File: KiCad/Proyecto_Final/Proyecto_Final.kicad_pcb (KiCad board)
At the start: 4 copper layers, 102 x 102 mm, 231 parts, among them J1 RF_IN, J10 PB, J11 PE, J12 PA, J13 PD, J14 SPI4, J15 OutEn, J16 CFG_SEL, J17 CTRL_MODE, J2 5v, J3 I2C1, J4 ARM SWD, J5 USB_B_Micro, J6 Boot_Select, J7 PG, J8 PC, J9 PF, Q1 Si2301CDS, SW1 Reset, T1 B0310J50100AHF, T2 B0310J50100AHF, T3 2450BL05A0100, U1 SKY13351, U10 MAX2837, U11 TLV1117-33, U12 USBLC6-2SC6, U13 STM32F723ZCTx, U14 5P49V5929, U2 RFFC5072, U3 SKY13351, U4 SKY13351, U5 SKY13351, U6 SKY13351, U7 SKY13351, U8 MAAL-010200, U9 MAX1193ETI+, Y1 25MHz

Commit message: Avances PCB.
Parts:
- removed J17: CTRL_MODE, Connector_PinHeader_2.54mm:PinHeader_2x01_P2.54mm_Vertical_SMD
- removed the R26 at (87.0, 53.6)
- removed R27, R28: 10k, Resistor_SMD:R_0402_1005Metric
- added H1: MountingHole, MountingHole:MountingHole_3.2mm_M3_Pad_Via, F.Cu at (53.6, 90.7)
- added H2: MountingHole, MountingHole:MountingHole_3.2mm_M3_Pad_Via, F.Cu at (80.0, 145.2)
- added H3: MountingHole, MountingHole:MountingHole_3.2mm_M3_Pad_Via, F.Cu at (61.5, 90.7)
- added H4: MountingHole, MountingHole:MountingHole_3.2mm_M3_Pad_Via, F.Cu at (171.3, 145.2)
- added JP1: SolderJumper, Jumper:SolderJumper-2_P1.3mm_Open_RoundedPad1.0x1.5mm, F.Cu at (127.1, 104.3)
- J16: value CFG_SEL -> CLK_OUT0; footprint Connector_PinHeader_2.54mm:PinHeader_2x04_P2.54mm_Vertical_SMD -> Tesis2020-21:RFSOLUTIONS_CON-SMA-EDGE-S
- R17, R18: value 10k -> 4.7k
- moved U11 98.2 mm to (96.4, 104.0)
- moved J3 76.3 mm to (154.0, 88.6), turned to 180 degrees
- moved J6 72.5 mm to (142.7, 78.9)
- moved R17 57.9 mm to (154.2, 91.2)
- moved R18 56.9 mm to (153.5, 92.3)
- moved J4 56.6 mm to (114.6, 79.0)
- moved J14 49.3 mm to (137.9, 67.0)
- moved J16 33.5 mm to (125.4, 78.4), turned to 270 degrees
- moved J15 19.7 mm to (114.2, 112.2), turned to 180 degrees
- moved U12 9.70 mm to (161.0, 139.1), turned to 90 degrees
- moved J5 8.95 mm to (160.2, 146.5)
- moved C109 6.35 mm to (119.8, 102.5), turned to 225 degrees
- moved R26 4.83 mm to (127.1, 100.9), turned to 90 degrees
- moved C110 4.81 mm to (119.3, 106.5), turned to 135 degrees
- moved R24 0.39 mm to (121.2, 111.8), turned to 45 degrees
- renumbered R29 to R26
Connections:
- J16 pad 2: Net-(J16-Pad1) -> GND
- R26 pad 1: Net-(R29-Pad1) -> Net-(JP1-Pad2)
- R26 pad 2: Clk_Out0 -> Net-(J16-Pad1)
- TP35 pad 1: Clk_Out0 -> Net-(J16-Pad1)
- U12 pad 1: USB_CONN_D+ -> USB_CONN_D-
- U12 pad 3: USB_CONN_D- -> USB_CONN_D+
- U12 pad 4: USB_D- -> USB_D+
- U12 pad 6: USB_D+ -> USB_D-
- U14 pad 24: Net-(R29-Pad1) -> Net-(JP1-Pad1)
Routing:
- net +5V: track 0.00 -> 144.6 mm, vias 0 -> 2
- net I2C1_SCL: track 3.01 -> 57.0 mm, vias 1 -> 2
- net I2C1_SDA: track 3.12 -> 56.1 mm, vias 1 -> 3
- net USB_D-: track 16.7 -> 37.0 mm
- net USB_D+: track 17.4 -> 37.6 mm
- net GND: track 113.7 -> 124.1 mm, vias 130 -> 135
- net Net-(J15-Pad1): track 0.00 -> 6.43 mm
- net USB_CONN_D+: track 0.00 -> 5.50 mm
- net USB_CONN_D-: track 0.00 -> 5.33 mm
- net Net-(JP1-Pad1): track 0.00 -> 3.86 mm
- net Net-(R29-Pad1): track 2.64 -> 0.00 mm
- net VDD: track 82.5 -> 84.8 mm, vias 32 -> 33
- net +3.3VA: track 14.2 -> 16.5 mm, vias 3 -> 4
- net XIN: track 5.66 -> 7.88 mm
- net Net-(JP1-Pad2): track 0.00 -> 2.19 mm
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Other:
- board size 102 x 102 mm -> 102 x 106.3 mm

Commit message: Avances PCB.
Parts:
- removed the J15 at (114.2, 112.2)
- removed the J2 at (41.9, 45.7)
- removed the J6 at (142.7, 78.9)
- added J14: OutEn, Connector_PinHeader_2.54mm:PinHeader_1x03_P2.54mm_Vertical, F.Cu at (111.6, 112.1)
- added J5: Boot_Select, Connector_PinHeader_2.54mm:PinHeader_1x03_P2.54mm_Vertical, F.Cu at (142.0, 92.9)
- H1, H2, H3, H4: value MountingHole -> MountingHole_Pad
- U11: value TLV1117-33 -> AMS1117-3.3
- moved FB1 112.4 mm to (99.4, 96.3), turned to 90 degrees
- moved C90 107.1 mm to (98.4, 98.7), turned to 180 degrees
- moved D1 99.8 mm to (103.6, 102.8), turned to 270 degrees
- moved C91 96.6 mm to (103.1, 106.7), turned to 180 degrees
- moved H2 90.9 mm to (170.9, 144.3)
- moved C95 89.5 mm to (103.4, 116.2)
- moved FB2 87.7 mm to (102.9, 114.5), turned to 270 degrees
- moved C94 85.5 mm to (103.4, 112.9)
- moved H3 79.3 mm to (99.0, 160.6)
- moved R15 79.1 mm to (169.3, 138.0), turned to 180 degrees
- moved C6 77.1 mm to (114.0, 138.5)
- moved H4 75.9 mm to (99.0, 168.5)
- moved SW1 74.8 mm to (134.2, 97.8), turned to 270 degrees
- moved J3 73.1 mm to (147.1, 144.5), turned to 90 degrees
- moved C7 65.1 mm to (116.3, 137.6), turned to 270 degrees
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- renumbered J11 to J10, J12 to J11, J13 to J12, J14 to J13, J16 to J15, J3 to J2, J4 to J3, J5 to J4, J7 to J6, J8 to J7, J9 to J8, J10 to J9
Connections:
- H1 pad 1: (no net) -> GND
- H2 pad 1: (no net) -> GND
- H3 pad 1: (no net) -> GND
- H4 pad 1: (no net) -> GND
- U13 pad 63: PE10 -> RESETX
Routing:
- net +3.3VA: track 16.5 -> 131.6 mm, vias 4 -> 6
- net RESETX: track 13.9 -> 87.6 mm, vias 2 -> 3
- net NRST: track 0.00 -> 29.1 mm, vias 0 -> 2
- net VDDA_CLK: track 20.3 -> 48.1 mm, vias 7 -> 8
- net GND: track 124.1 -> 148.5 mm, vias 135 -> 142
- net VDD: track 84.8 -> 107.8 mm, vias 33 -> 58
- net BOOT0: track 0.00 -> 9.52 mm, vias 0 -> 2
- net Net-(C90-Pad1): track 0.00 -> 9.49 mm
- net USB_D+: track 37.6 -> 34.1 mm
- net Net-(J5-Pad2): track 0.00 -> 3.15 mm
- net USB_D-: track 37.0 -> 34.1 mm
- net Net-(D2-Pad1): track 0.00 -> 1.98 mm
- net Net-(J14-Pad2): track 6.43 -> 8.34 mm
- net +5V: track 144.6 -> 142.7 mm, vias 2 -> 3

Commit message: Avances PCB.
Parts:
- removed the C13 at (100.2, 65.4)
- removed the C99 at (131.4, 69.3)
- removed the TP21 at (279.4, 17.8)
- removed the TP22 at (271.8, 38.1)
- removed the TP23 at (256.5, 27.9)
- removed the TP24 at (248.9, 22.9)
- added C52: 100nF, Capacitor_SMD:C_0402_1005Metric, F.Cu at (134.3, 92.8)
- added C76: 33pF, Capacitor_SMD:C_0402_1005Metric, F.Cu at (119.6, 141.1)
- moved TP16 197.1 mm to (123.9, 144.0)
- moved TP14 187.1 mm to (121.4, 144.3)
- moved TP17 187.1 mm to (106.9, 115.6)
- moved TP19 185.6 mm to (108.0, 104.2)
- moved TP13 183.6 mm to (118.8, 144.3)
- moved TP18 165.1 mm to (99.4, 93.6)
- moved TP27 161.1 mm to (135.0, 108.1)
- moved TP30 160.8 mm to (121.4, 115.7)
- moved TP15 160.4 mm to (116.3, 143.7)
- moved TP31 160.2 mm to (128.9, 100.4)
- moved TP29 154.1 mm to (127.2, 116.8)
- moved TP28 153.8 mm to (133.5, 119.2)
- moved TP20 148.7 mm to (99.4, 110.9)
- moved TP12 141.0 mm to (127.5, 143.9)
- moved TP22 132.7 mm to (146.2, 88.7)
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- renumbered C48 to C1, C57 to C10, C37 to C100, C38 to C101, C39 to C102, C40 to C103, C41 to C104, C42 to C105, C43 to C106, C44 to C107, C45 to C108, C46 to C109, C58 to C11, C47 to C110, C59 to C12, C60 to C13, C61 to C14, C62 to C15, C63 to C16, C64 to C17, C65 to C18, C66 to C19, C49 to C2, C67 to C20, C68 to C21, C69 to C22, C70 to C23, C71 to C24, C72 to C25, C73 to C26, C74 to C27, C75 to C28, C76 to C29, C50 to C3, C77 to C30, C78 to C31, C79 to C32, C80 to C33, C81 to C34, C82 to C35, C83 to C36, C84 to C37, C85 to C38, C86 to C39, C51 to C4, C87 to C40, C88 to C41, C89 to C42, C90 to C43, C91 to C44, C92 to C45, C93 to C46, C94 to C47, C95 to C48, C96 to C49, C52 to C5, C97 to C50, C98 to C51, C100 to C53, C101 to C54, C102 to C55, C103 to C56, C104 to C57, C105 to C58, C106 to C59, C53 to C6, C107 to C60, C108 to C61, C109 to C62, C110 to C63, C1 to C64, C2 to C65, C3 to C66, C4 to C67, C5 to C68, C6 to C69, C54 to C7, C7 to C70, C8 to C71, C9 to C72, C10 to C73, C11 to C74, C12 to C75, C14 to C77, C15 to C78, C16 to C79, C55 to C8, C17 to C80, C18 to C81, C19 to C82, C20 to C83, C21 to C84, C22 to C85, C23 to C86, C24 to C87, C25 to C88, C26 to C89, C56 to C9, C27 to C90, C28 to C91, C29 to C92, C30 to C93, C31 to C94, C32 to C95, C33 to C96, C34 to C97, C35 to C98, C36 to C99, J2 to J1, J11 to J10, J12 to J11, J13 to J12, J14 to J13, J15 to J14, J1 to J15, J3 to J2, J4 to J3, J5 to J4, J6 to J5, J7 to J6, J8 to J7, J9 to J8, J10 to J9, L4 to L1, L1 to L2, L2 to L3, L3 to L4, R7 to R1, R16 to R10, R17 to R11, R18 to R12, R19 to R13, R20 to R14, R21 to R15, R22 to R16, R23 to R17, R24 to R18, R25 to R19, R8 to R2, R26 to R20, R1 to R21, R2 to R22, R3 to R23, R4 to R24, R5 to R25, R6 to R26, R9 to R3, R10 to R4, R11 to R5, R12 to R6, R13 to R7, R14 to R8, R15 to R9, T3 to T1, T1 to T2, T2 to T3, TP25 to TP21, TP26 to TP22, TP27 to TP23, TP28 to TP24, TP29 to TP25, TP30 to TP26, TP31 to TP27, TP32 to TP28, TP33 to TP29, TP34 to TP30, TP35 to TP31, TP36 to TP32, TP37 to TP33, TP38 to TP34, TP39 to TP35, TP40 to TP36, TP41 to TP37, TP42 to TP38, TP43 to TP39, TP44 to TP40, TP45 to TP41, U9 to U1, U4 to U10, U5 to U11, U6 to U12, U7 to U13, U8 to U14, U10 to U2, U11 to U3, U12 to U4, U13 to U5, U14 to U6, U1 to U7, U2 to U8, U3 to U9
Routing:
- net SWCLK: track 0.00 -> 58.4 mm, vias 0 -> 2
- net SWDIO: track 0.00 -> 58.4 mm, vias 0 -> 2
- net SWO: track 0.00 -> 56.7 mm, vias 0 -> 2
- net NRST: track 29.1 -> 68.7 mm, vias 2 -> 4
- net SPI1_CS1: track 40.6 -> 58.3 mm
- net SPI1_MISO: track 70.5 -> 85.3 mm, vias 5 -> 8
- net SPI1_MOSI: track 74.0 -> 87.3 mm, vias 3 -> 6
- net SPI1_CS0: track 71.2 -> 83.3 mm, vias 4 -> 5
- net GND: track 148.5 -> 160.1 mm, vias 142 -> 147
- net SPI1_SCK: track 77.7 -> 84.7 mm
- net I2C1_SDA: track 56.1 -> 61.5 mm
- net I2C1_SCL: track 57.0 -> 62.2 mm
- net +3.3VA: track 131.6 -> 136.2 mm
- net VDD: track 107.8 -> 110.3 mm
- net MCU_CLK: track 35.0 -> 37.4 mm
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
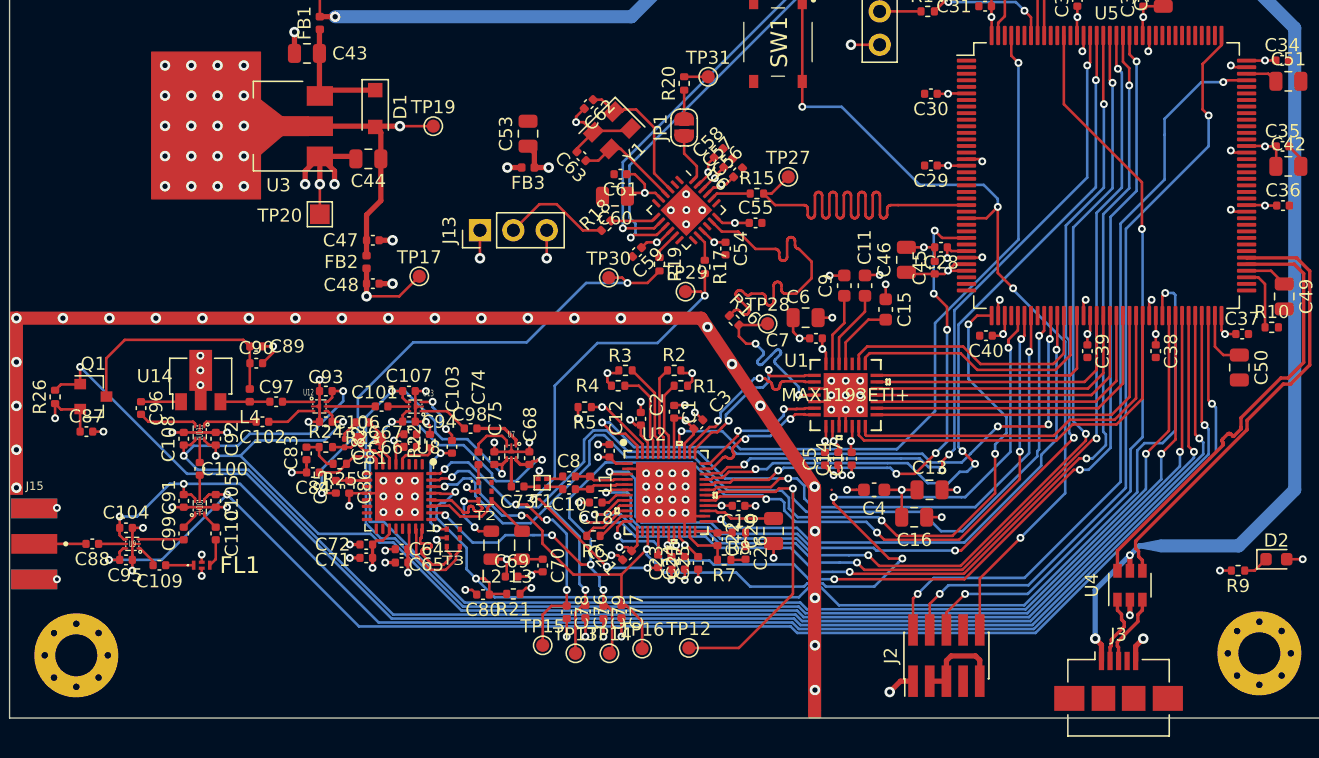
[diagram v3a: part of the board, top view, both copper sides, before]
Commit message: Aumentado clearance a 0.2mm
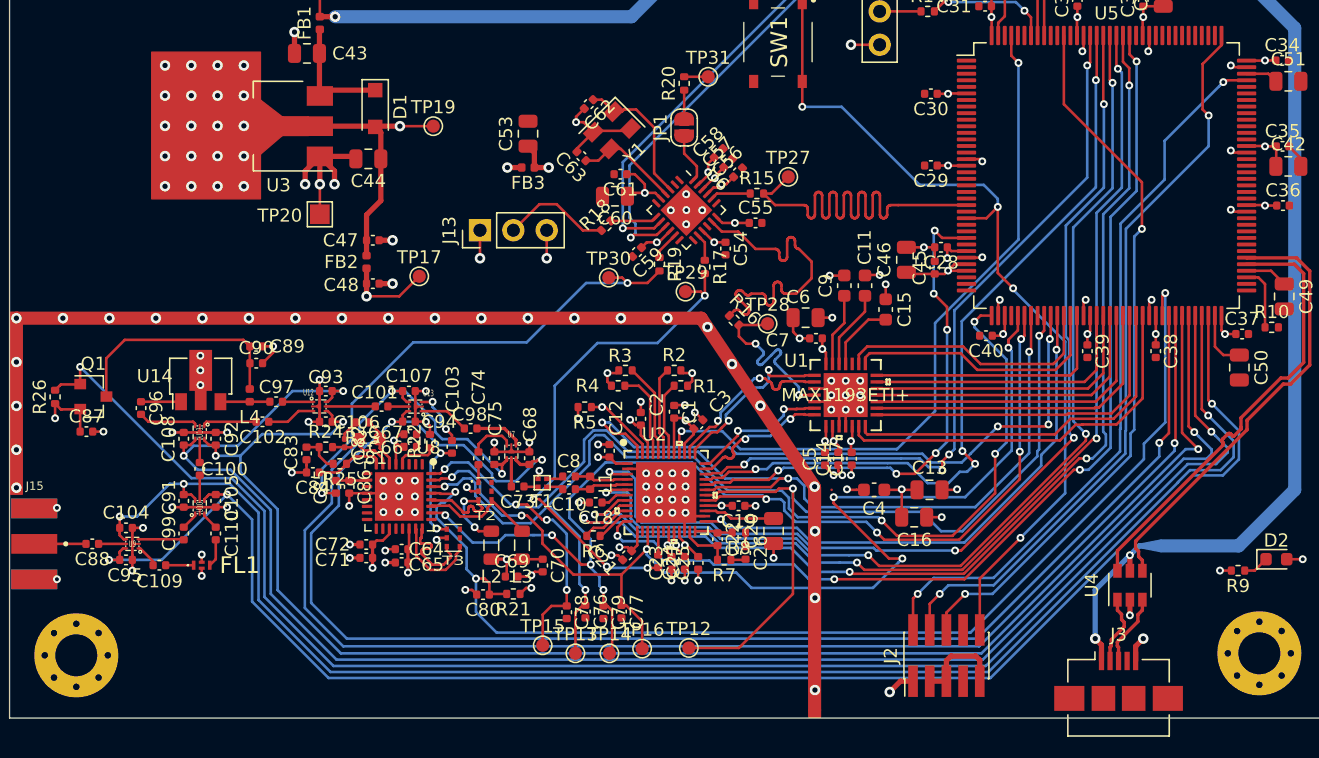
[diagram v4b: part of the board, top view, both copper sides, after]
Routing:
- net Rx_Mix: track 106.8 -> 118.5 mm
- net Rx_Mix_Bypass: track 106.4 -> 117.4 mm
- net Filt_Bypass: track 108.8 -> 118.3 mm
- net Filtro: track 111.1 -> 120.3 mm
- net Rx_Amp_Pwr: track 113.2 -> 122.1 mm
- net Rx_Amp_Bypass: track 107.6 -> 115.3 mm
- net Rx_Amp: track 116.8 -> 124.3 mm
- net GND: track 160.1 -> 154.7 mm, vias 147 -> 142
- net SWDIO: track 58.4 -> 56.0 mm
- net SWO: track 56.7 -> 55.1 mm
- net SWCLK: track 58.4 -> 56.9 mm
- net SPI1_CS0: track 83.3 -> 82.8 mm
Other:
- net class Default: clearance 0.1 -> 0.2
- rule trace_clearance: 0.1 -> 0.2

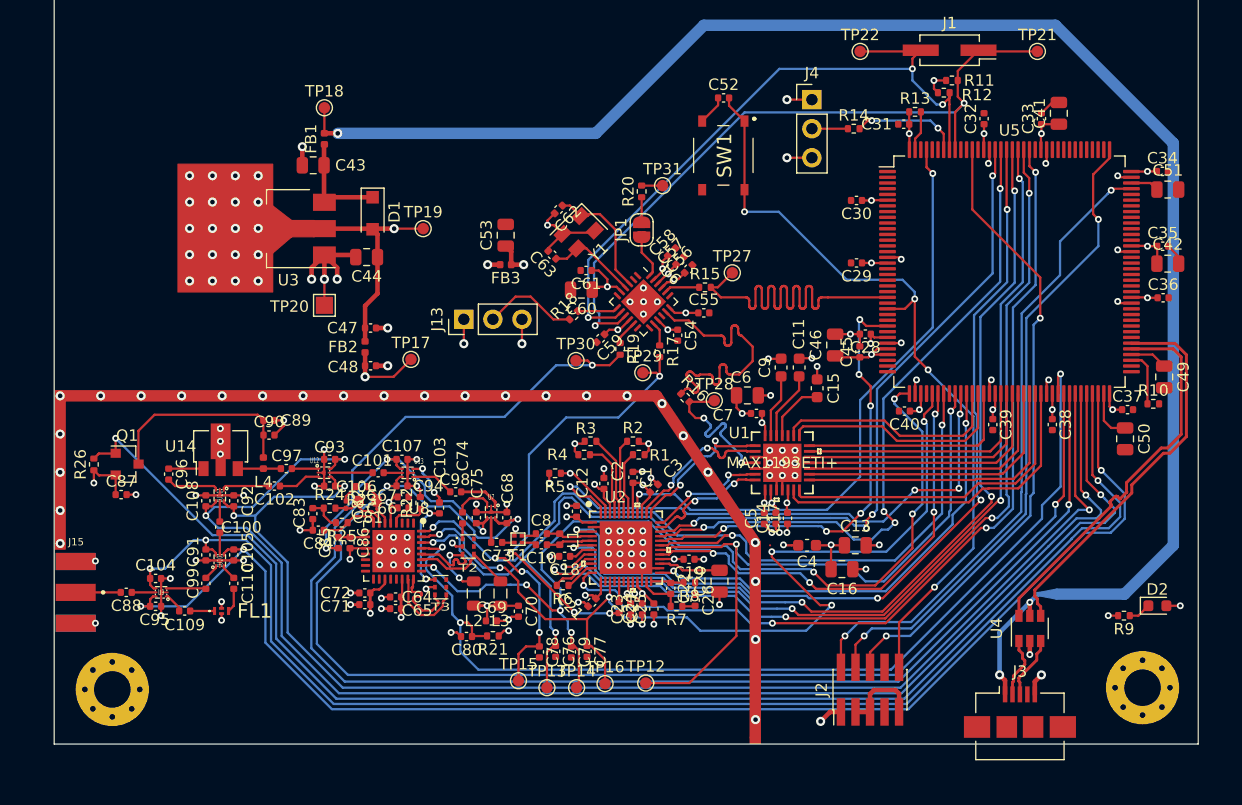
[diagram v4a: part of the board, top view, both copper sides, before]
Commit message: Eliminadas conexiones innecesarias del transceptor.
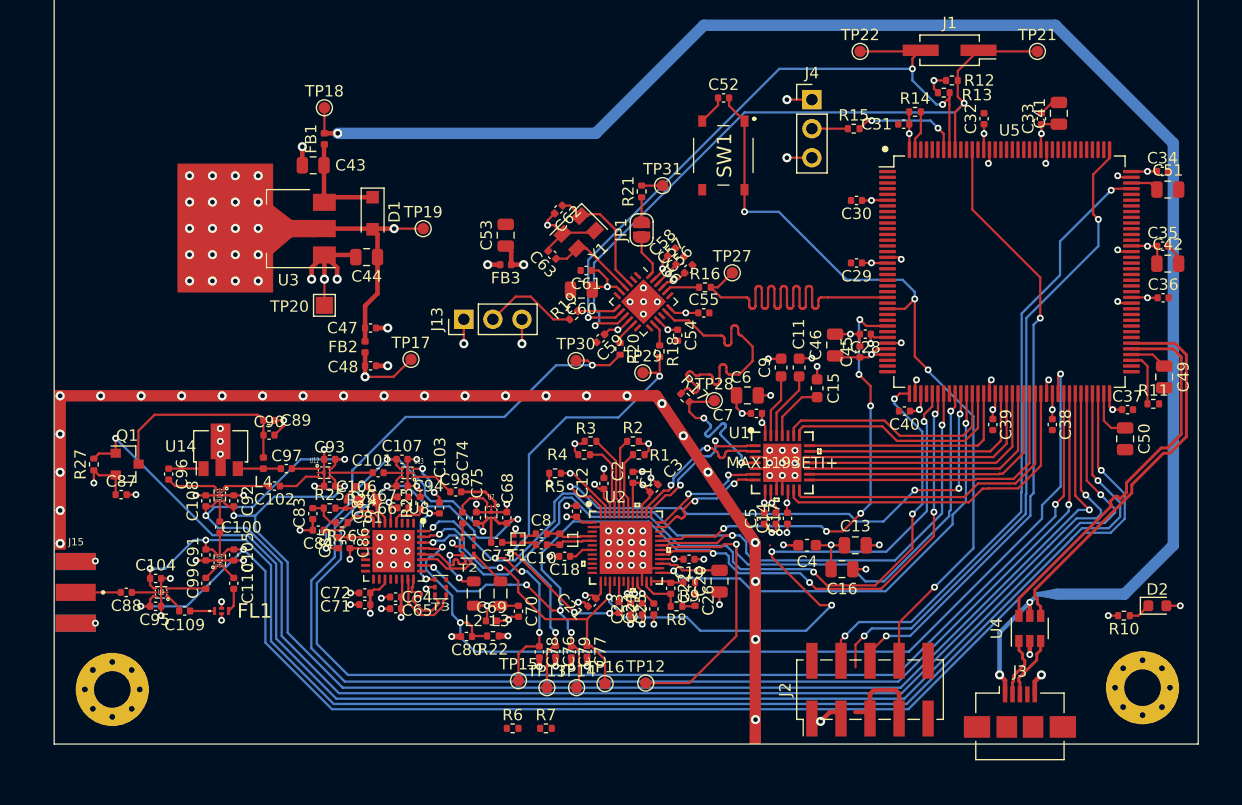
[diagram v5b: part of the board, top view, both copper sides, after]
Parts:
- added R7: 49.9 1%, Resistor_SMD:R_0402_1005Metric, F.Cu at (118.7, 147.9)
- J2: footprint Connector_PinHeader_1.27mm:PinHeader_2x05_P1.27mm_Vertical_SMD -> Connector_PinHeader_2.54mm:PinHeader_2x05_P2.54mm_Vertical_SMD
- R6: value 100 -> 49.9 1%
- moved R6 13.2 mm to (115.8, 147.9), turned to 0 degrees
- renumbered R9 to R10, R10 to R11, R11 to R12, R12 to R13, R13 to R14, R14 to R15, R15 to R16, R16 to R17, R17 to R18, R18 to R19, R19 to R20, R20 to R21, R21 to R22, R22 to R23, R23 to R24, R24 to R25, R25 to R26, R26 to R27, R7 to R8, R8 to R9
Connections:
- R6 pad 2: Net-(R6-Pad2) -> GND
- U2 pad 10: Net-(R6-Pad2) -> Net-(R6-Pad1)
- U2 pad 11: Net-(R6-Pad1) -> Net-(R7-Pad2)
- U2 pad 12: B1 -> Net-(U2-Pad12)
- U2 pad 3: B5 -> Net-(U2-Pad3)
- U2 pad 33: B7 -> Net-(U2-Pad33)
- U2 pad 34: B6 -> Net-(U2-Pad34)
- U2 pad 6: B4 -> Net-(U2-Pad6)
- U2 pad 8: B3 -> Net-(U2-Pad8)
- U2 pad 9: B2 -> Net-(U2-Pad9)
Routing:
- net B2: track 81.8 -> 0.00 mm, vias 4 -> 0
- net B3: track 78.9 -> 0.00 mm, vias 4 -> 0
- net B4: track 78.1 -> 0.00 mm, vias 4 -> 0
- net B1: track 77.5 -> 0.00 mm, vias 4 -> 0
- net B5: track 76.6 -> 0.00 mm, vias 4 -> 0
- net B7: track 59.6 -> 0.00 mm, vias 4 -> 0
- net B6: track 56.7 -> 0.00 mm, vias 4 -> 0
- net RXHP: track 54.3 -> 0.00 mm, vias 2 -> 0
- net GND: track 154.7 -> 159.9 mm, vias 142 -> 147
- net Net-(R6-Pad2): track 3.94 -> 0.00 mm
- net Net-(R6-Pad1): track 2.70 -> 0.00 mm
- net VDD: track 110.4 -> 108.0 mm, vias 58 -> 57
- net RESETX: track 88.5 -> 86.5 mm
